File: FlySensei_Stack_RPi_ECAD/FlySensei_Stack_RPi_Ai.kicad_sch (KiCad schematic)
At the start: 7 parts, among them U4 G313-06329-00

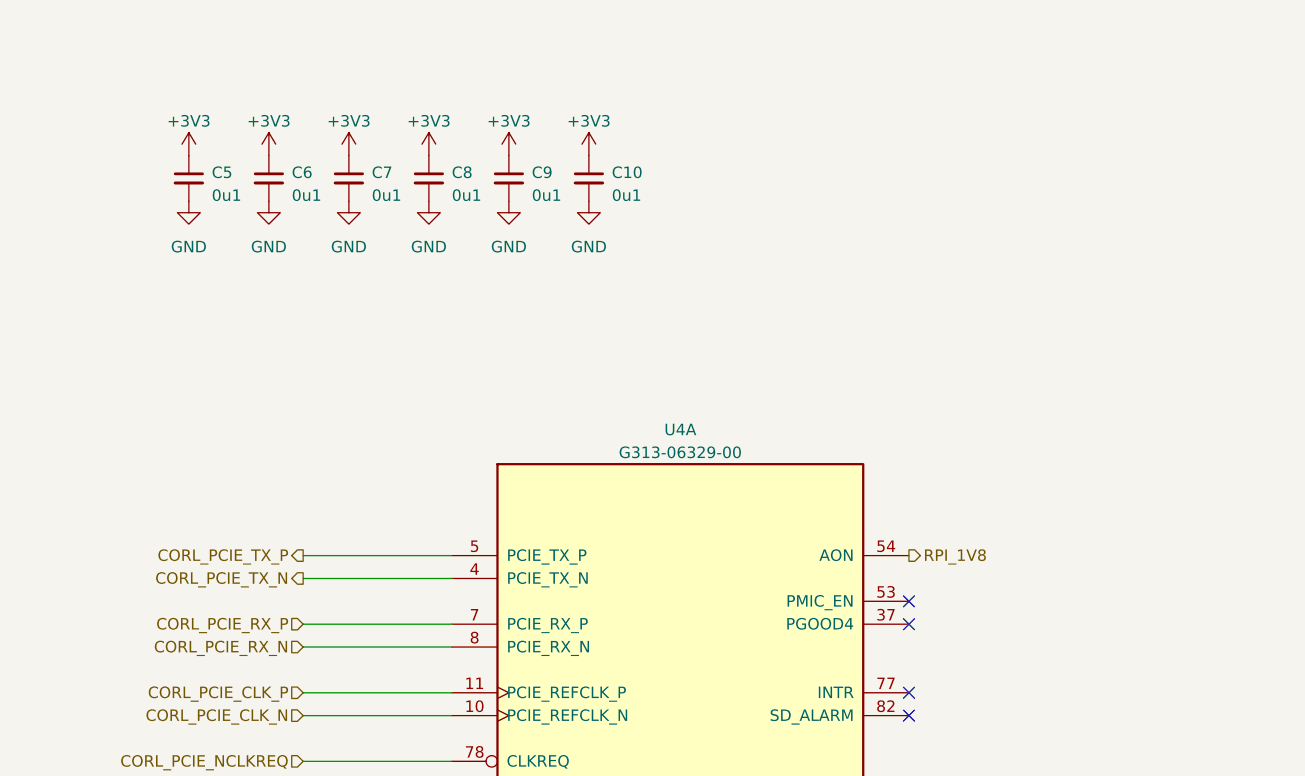
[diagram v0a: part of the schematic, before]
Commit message: PCB Design for the Raspberry PI CM4 Board (V0.1)
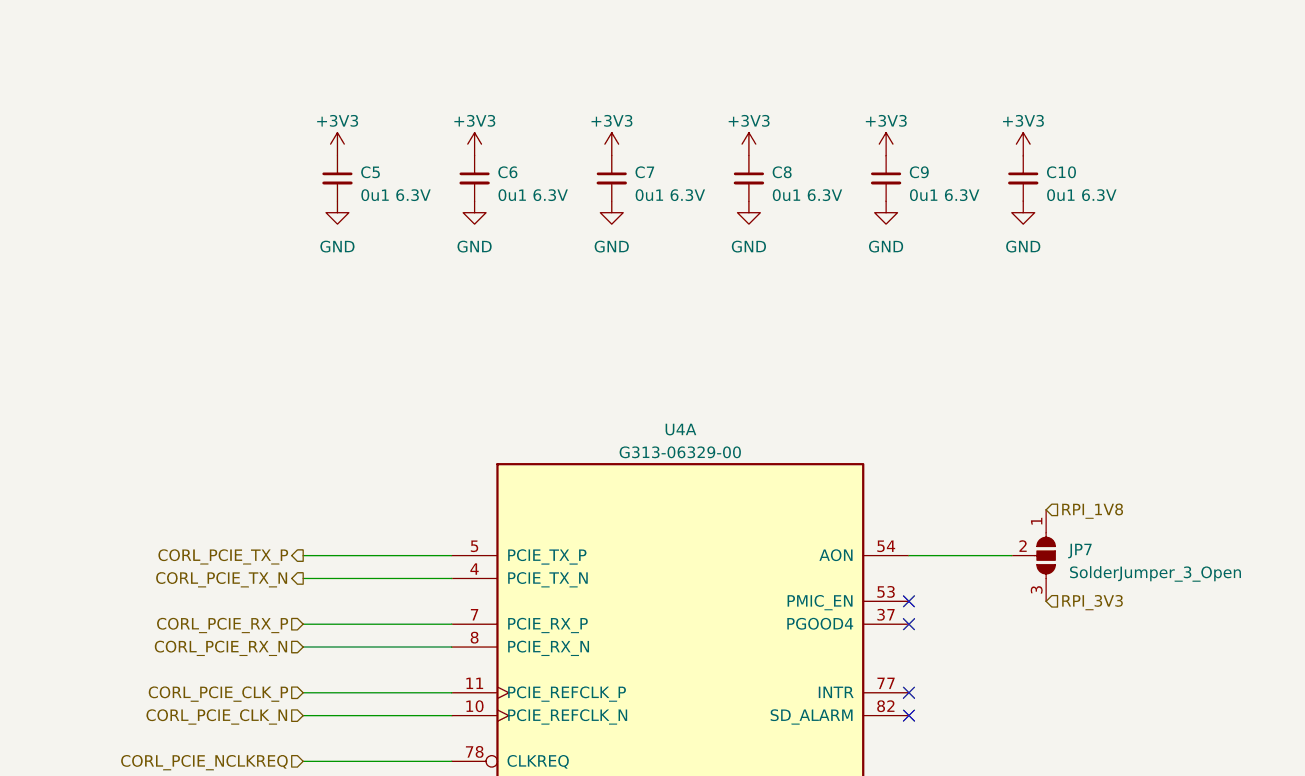
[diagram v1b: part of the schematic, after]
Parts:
- added JP7: SolderJumper_3_Open, Jumper:SolderJumper-3_P1.3mm_Open_RoundedPad1.0x1.5mm, symbol Jumper:SolderJumper_3_Open
- C10, C5, C6, C7, C8, C9: value 0u1 -> 0u1 6.3V; footprint (none) -> Capacitor_SMD:C_0402_1005Metric
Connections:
- net RPI_1V8: now also JP7.1 (A); no longer U4.54 (AON)
- new net: JP7.2 (C), U4.54 (AON)
- new net RPI_3V3: JP7.3 (B)
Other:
- moved on the sheet: C10, C5, C6, C7, C8, C9
